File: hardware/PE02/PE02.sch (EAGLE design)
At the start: 27 parts, among them IC1 MSP430G2231, IC2 TPS78222, J1 78171-0002

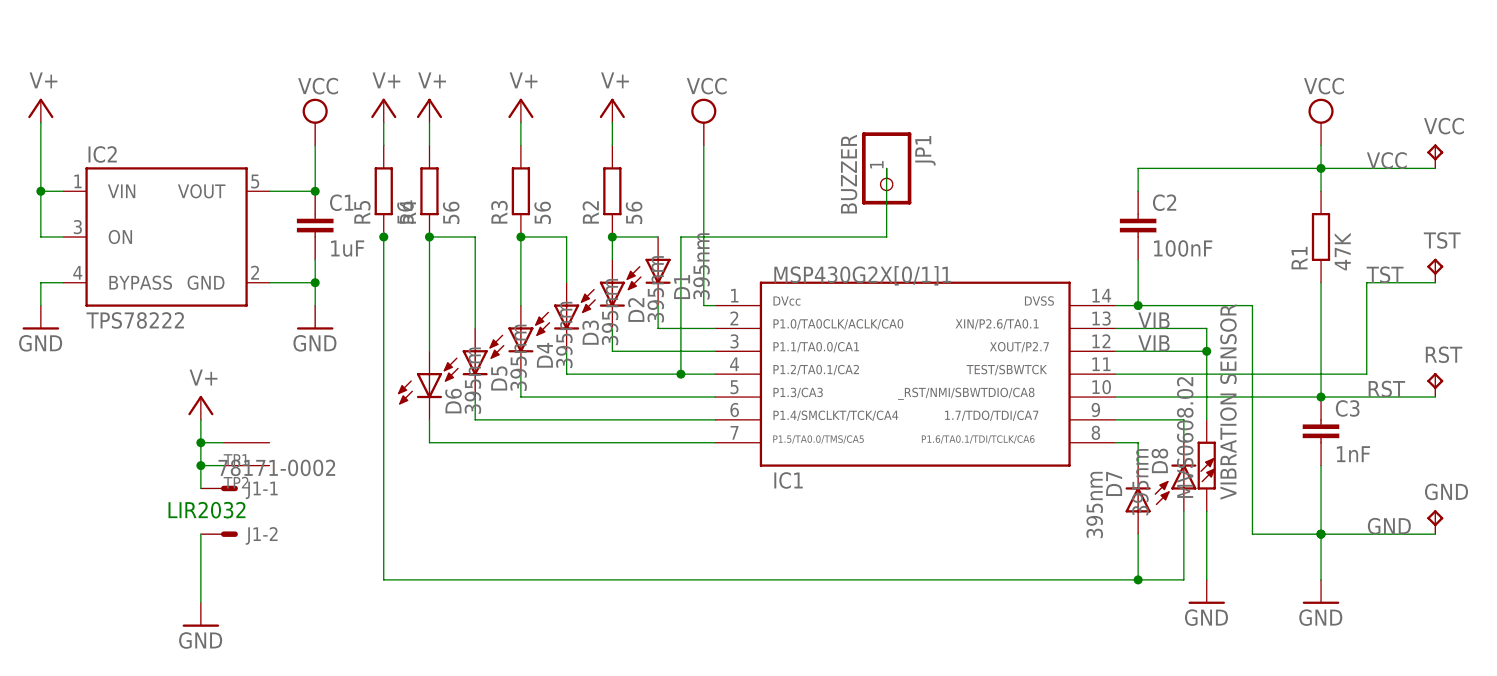
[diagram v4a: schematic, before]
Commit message: removed sewtab, buzzer hole
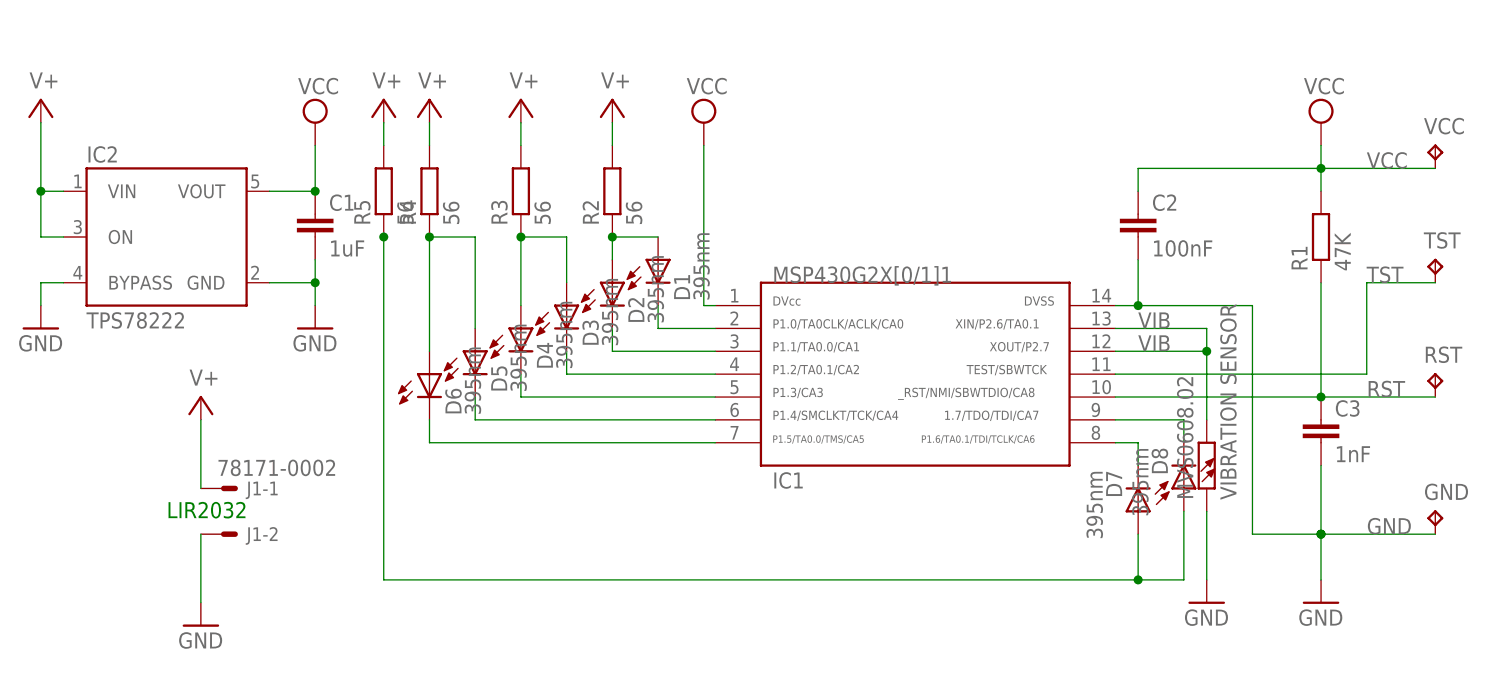
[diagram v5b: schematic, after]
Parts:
- removed JP1: BUZZER, adafruit:PINHD-1X1CB
- removed TP1, TP2: SEWTAP0.4IN, adafruit:SEWTAP0.4IN
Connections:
- removed net N$6: D3.C, IC1.4, JP1.1
- new net N$7: D3.C, IC1.4
- net V+: no longer TP1.SEW, TP2.SEW
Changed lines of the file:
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@@
 <part name="RST" library="testpad" deviceset="TP" device="TP10R" value="TPTP10R"/>
 <part name="GND" library="testpad" deviceset="TP" device="TP10R" value="TPTP10R"/>
-<part name="TP1" library="adafruit" deviceset="SEWTAP" device="0.4IN"/>
-<part name="TP2" library="adafruit" deviceset="SEWTAP" device="0.4IN"/>
-<part name="JP1" library="adafruit" deviceset="PINHD-1X1" device="CB" value="BUZZER"/>
 <part name="MVS0608.02" library="rcl" deviceset="R-EU_" device="R1210" value="VIBRATION SENSOR"/>
 <part name="GND5" library="supply1" deviceset="GND" device=""/>
@@
 <instance part="RST" gate="G$1" x="104.14" y="58.42"/>
 <instance part="GND" gate="G$1" x="104.14" y="43.18"/>
-<instance part="TP1" gate="G$1" x="-30.48" y="50.8" rot="R180"/>
-<instance part="TP2" gate="G$1" x="-30.48" y="48.26" rot="R180"/>
-<instance part="JP1" gate="G$1" x="43.18" y="78.74" rot="R270"/>
 <instance part="MVS0608.02" gate="G$1" x="78.74" y="48.26" rot="R90"/>
 <instance part="GND5" gate="1" x="78.74" y="33.02"/>
@@
 </segment>
 </net>
-<net name="N$6" class="0">
-<segment>
-<pinref part="IC1" gate="G$1" pin="4"/>
-<pinref part="D3" gate="LED" pin="C"/>
-<wire x1="24.13" y1="58.42" x2="20.32" y2="58.42" width="0.1524" layer="91"/>
-<wire x1="20.32" y1="58.42" x2="7.62" y2="58.42" width="0.1524" layer="91"/>
-<wire x1="7.62" y1="58.42" x2="7.62" y2="60.96" width="0.1524" layer="91"/>
-<junction x="20.32" y="58.42"/>
-<pinref part="JP1" gate="G$1" pin="1"/>
-<wire x1="43.18" y1="81.28" x2="43.18" y2="73.66" width="0.1524" layer="91"/>
-<wire x1="43.18" y1="73.66" x2="20.32" y2="73.66" width="0.1524" layer="91"/>
-<wire x1="20.32" y1="58.42" x2="20.32" y2="73.66" width="0.1524" layer="91"/>
-</segment>
-</net>
 <net name="N$8" class="0">
 <segment>
@@
 <segment>
 <pinref part="SUPPLY2" gate="1" pin="V+"/>
-<wire x1="-33.02" y1="48.26" x2="-33.02" y2="50.8" width="0.1524" layer="91"/>
-<junction x="-33.02" y="50.8"/>
-<wire x1="-33.02" y1="50.8" x2="-33.02" y2="53.34" width="0.1524" layer="91"/>
-<wire x1="-30.48" y1="50.8" x2="-33.02" y2="50.8" width="0.1524" layer="91"/>
-<pinref part="TP1" gate="G$1" pin="SEW"/>
-<pinref part="TP2" gate="G$1" pin="SEW"/>
-<wire x1="-30.48" y1="48.26" x2="-33.02" y2="48.26" width="0.1524" layer="91"/>
-<wire x1="-33.02" y1="45.72" x2="-33.02" y2="48.26" width="0.1524" layer="91"/>
-<junction x="-33.02" y="48.26"/>
+<wire x1="-33.02" y1="45.72" x2="-33.02" y2="53.34" width="0.1524" layer="91"/>
 <pinref part="J1" gate="-1" pin="S"/>
 </segment>
@@
 </segment>
 </net>
+<net name="N$7" class="0">
+<segment>
+<pinref part="D3" gate="LED" pin="C"/>
+<pinref part="IC1" gate="G$1" pin="4"/>
+<wire x1="24.13" y1="58.42" x2="7.62" y2="58.42" width="0.1524" layer="91"/>
+<wire x1="7.62" y1="58.42" x2="7.62" y2="60.96" width="0.1524" layer="91"/>
+</segment>
+</net>

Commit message: Added piezo buzzer circuit
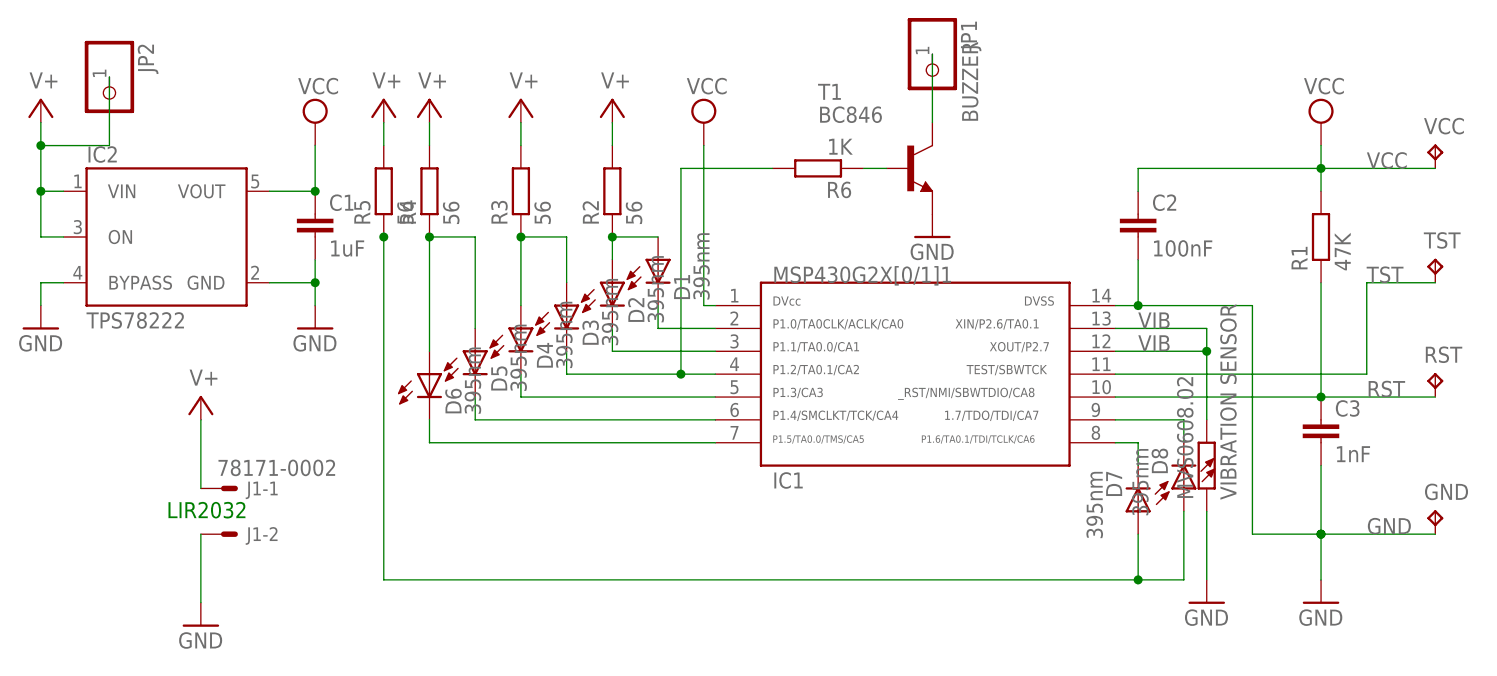
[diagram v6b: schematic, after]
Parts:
- added JP1, JP2: (no value), adafruit:PINHD-1X1CB
- added R6: 1K, rcl:R-EU_R0603
- added T1: BC846, transistor:BC846
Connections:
- new net BUZZER: JP1.1, T1.C
- new net N$9: R6.1, T1.B
- net GND: now also T1.E
- net N$7: now also R6.2
- net V+: now also JP2.1
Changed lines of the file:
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@@
 <part name="C1" library="SparkFun" deviceset="CAP" device="0805" value="1uF"/>
 <part name="J1" library="con-molex-pico-ezmate" deviceset="78171-0002" device=""/>
+<part name="T1" library="transistor" deviceset="BC846" device=""/>
+<part name="JP1" library="adafruit" deviceset="PINHD-1X1" device="CB"/>
+<part name="JP2" library="adafruit" deviceset="PINHD-1X1" device="CB"/>
+<part name="GND6" library="supply1" deviceset="GND" device=""/>
+<part name="R6" library="rcl" deviceset="R-EU_" device="R0603" value="1K"/>
 </parts>
 <sheets>
@@
 <instance part="J1" gate="-1" x="-30.48" y="45.72"/>
 <instance part="J1" gate="-2" x="-30.48" y="40.64"/>
+<instance part="T1" gate="G$1" x="45.72" y="81.28"/>
+<instance part="JP1" gate="G$1" x="48.26" y="91.44" rot="R270"/>
+<instance part="JP2" gate="G$1" x="-43.18" y="88.9" rot="R270"/>
+<instance part="GND6" gate="1" x="48.26" y="73.66"/>
+<instance part="R6" gate="G$1" x="35.56" y="81.28" rot="R180"/>
 </instances>
 <busses>
@@
 <pinref part="J1" gate="-2" pin="S"/>
 </segment>
+<segment>
+<pinref part="T1" gate="G$1" pin="E"/>
+<pinref part="GND6" gate="1" pin="GND"/>
+</segment>
 </net>
 <net name="VIB" class="0">
@@
 <pinref part="SUPPLY3" gate="1" pin="V+"/>
 <wire x1="-48.26" y1="78.74" x2="-50.8" y2="78.74" width="0.1524" layer="91"/>
-<wire x1="-50.8" y1="78.74" x2="-50.8" y2="86.36" width="0.1524" layer="91"/>
+<wire x1="-50.8" y1="78.74" x2="-50.8" y2="83.82" width="0.1524" layer="91"/>
 <pinref part="IC2" gate="A" pin="ON"/>
+<wire x1="-50.8" y1="83.82" x2="-50.8" y2="86.36" width="0.1524" layer="91"/>
 <wire x1="-48.26" y1="73.66" x2="-50.8" y2="73.66" width="0.1524" layer="91"/>
 <wire x1="-50.8" y1="73.66" x2="-50.8" y2="78.74" width="0.1524" layer="91"/>
 <junction x="-50.8" y="78.74"/>
+<pinref part="JP2" gate="G$1" pin="1"/>
+<wire x1="-43.18" y1="91.44" x2="-43.18" y2="83.82" width="0.1524" layer="91"/>
+<wire x1="-43.18" y1="83.82" x2="-50.8" y2="83.82" width="0.1524" layer="91"/>
+<junction x="-50.8" y="83.82"/>
 </segment>
 <segment>
@@
 <pinref part="D3" gate="LED" pin="C"/>
 <pinref part="IC1" gate="G$1" pin="4"/>
-<wire x1="24.13" y1="58.42" x2="7.62" y2="58.42" width="0.1524" layer="91"/>
+<wire x1="24.13" y1="58.42" x2="20.32" y2="58.42" width="0.1524" layer="91"/>
+<wire x1="20.32" y1="58.42" x2="7.62" y2="58.42" width="0.1524" layer="91"/>
 <wire x1="7.62" y1="58.42" x2="7.62" y2="60.96" width="0.1524" layer="91"/>
-</segment>
-</net>
+<junction x="20.32" y="58.42"/>
+<pinref part="R6" gate="G$1" pin="2"/>
+<wire x1="20.32" y1="81.28" x2="30.48" y2="81.28" width="0.1524" layer="91"/>
+<wire x1="20.32" y1="58.42" x2="20.32" y2="81.28" width="0.1524" layer="91"/>
+</segment>
+</net>
+<net name="BUZZER" class="0">
+<segment>
+<pinref part="JP1" gate="G$1" pin="1"/>
+<pinref part="T1" gate="G$1" pin="C"/>
+<wire x1="48.26" y1="93.98" x2="48.26" y2="86.36" width="0.1524" layer="91"/>
+<label x="53.34" y="86.36" size="1.778" layer="95" rot="R90"/>
+</segment>
+</net>
+<net name="N$9" class="0">
+<segment>
+<pinref part="T1" gate="G$1" pin="B"/>
+<pinref part="R6" gate="G$1" pin="1"/>
+<wire x1="43.18" y1="81.28" x2="40.64" y2="81.28" width="0.1524" layer="91"/>
+</segment>
+</net>
